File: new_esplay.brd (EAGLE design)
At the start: 100 x 50 mm, 96 parts, among them J3 AUDIO_JACK_3.5MM_KIT, Q1 1.1A/60V/600mΩ, T1 2n2222, T2 2n2222, T3 2n2222, U2 MIC5219 3.3V

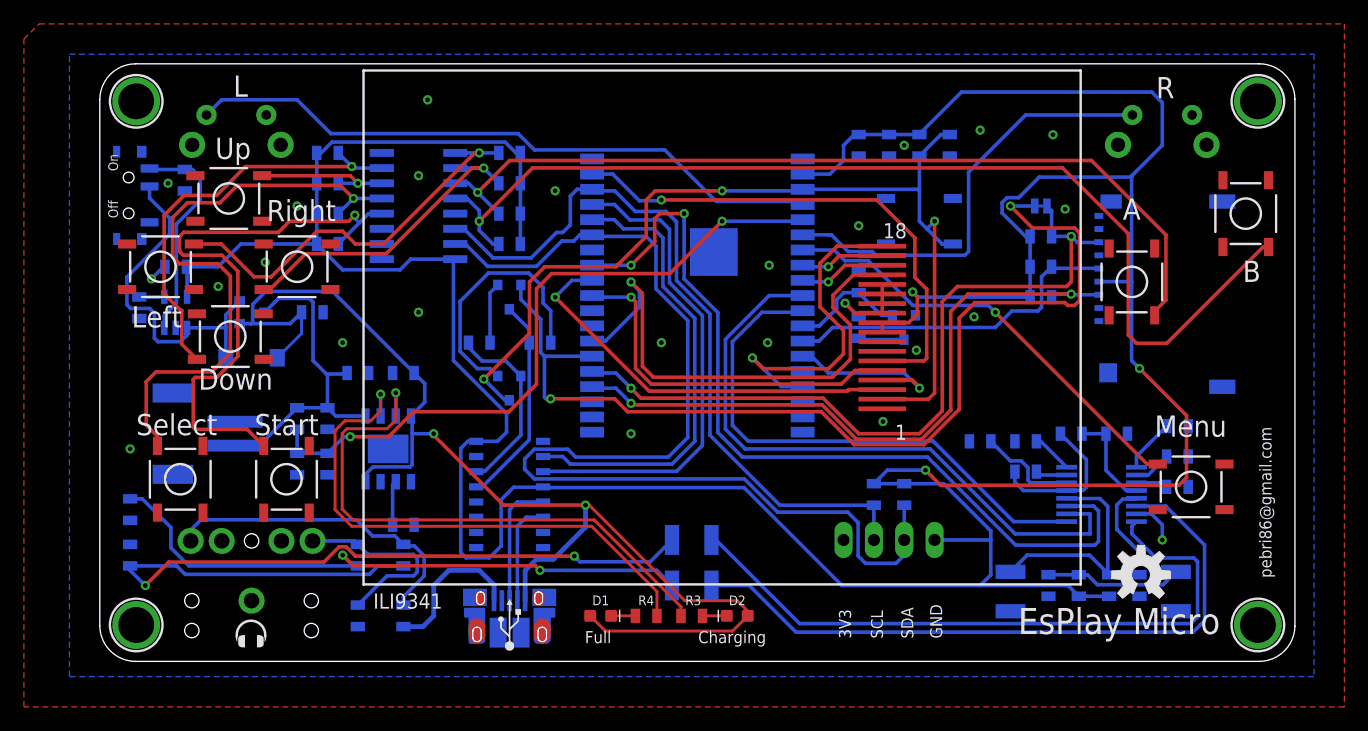
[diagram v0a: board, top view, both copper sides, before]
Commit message: Optimize vias and add amplifier
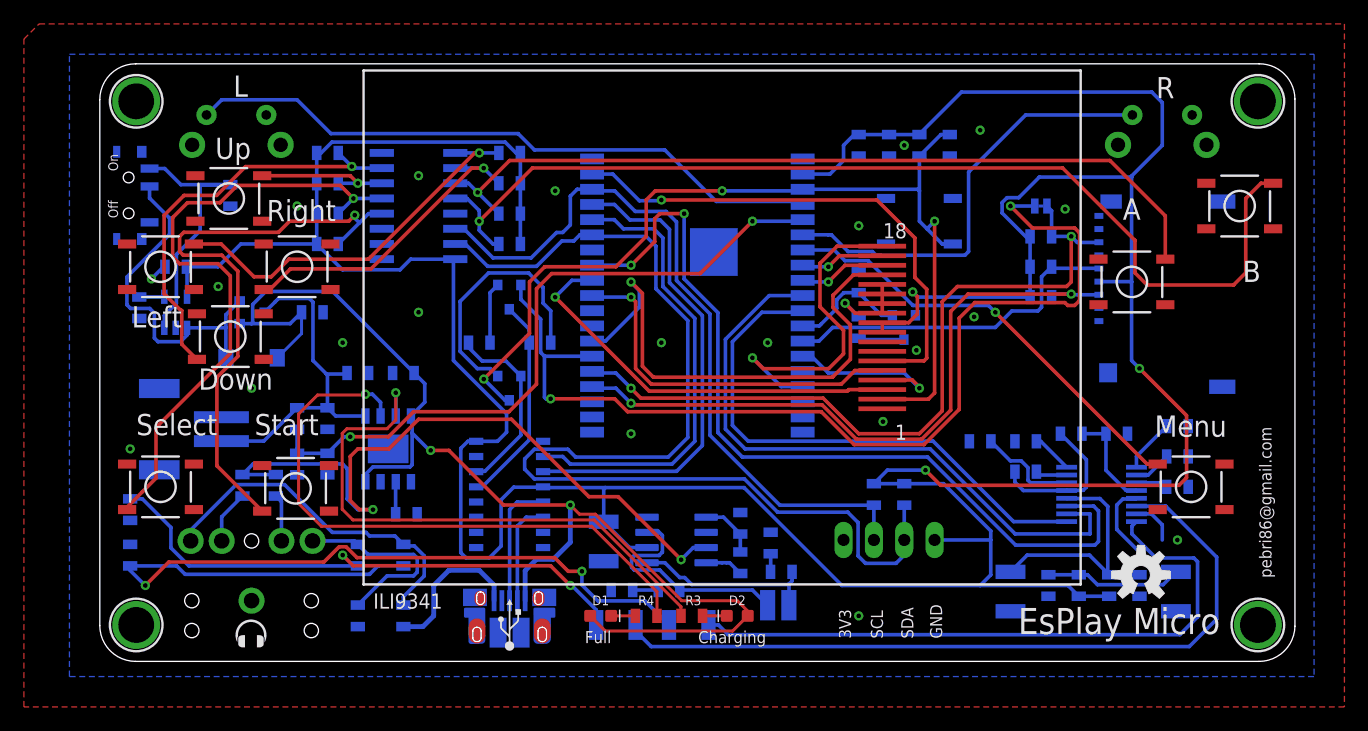
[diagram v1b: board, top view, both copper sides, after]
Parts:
- added C18: 47uF, SparkFun-Capacitors:EIA3528
- added C19: 10uF, SparkFun-Capacitors:0805
- added C20: 0.01uF, SparkFun-Capacitors:0805
- added C21, C24: 0.1uF, SparkFun-Capacitors:0805
- added R38, R41: 4,7, SparkFun-Resistors:0805
- added R39, R40: 100, SparkFun-Resistors:0805
- added SPK+, SPK-: (no value), wirepad:SMD1,27-2,54
- added U1: TDA2822MSOIC8, TDA2822M:SOIC127P600X175-8N
- moved C10 7.16 mm to (43.2, 3.05)
- moved C11 7.12 mm to (49.3, 3.05)
- moved R5 4.02 mm to (10.9, 39.0)
- moved S8 1.77 mm to (5.08, 14.6), turned to 0 degrees
- moved J2 1.20 mm to (6.48, 19.4)
- moved S7 1.08 mm to (16.4, 14.5), turned to 0 degrees
- moved R2 0.92 mm to (25.7, 12.3)
- moved S10 0.81 mm to (95.4, 38.1), turned to 180 degrees
- turned S9 to 180 degrees
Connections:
- removed net EXP: ESP32-WROVER.39
- new net N$15: J3.RSH, R39.1
- new net N$16: J3.TSH, R40.1
- new net N$17: R39.2, R40.2, U1.7
- new net N$23: C19.2, C20.1, U1.5
- new net N$30: C19.1, U1.8
- new net N$31: C24.1, SPK+.1, U1.1
- new net N$32: C21.1, SPK-.1, U1.3
- new net N$33: C21.2, R38.1
- new net N$34: C24.2, R41.1
- net 3V3: now also C18.A, U1.2
- net GND: now also C18.C, C20.2, ESP32-WROVER.39, J1.SHIELD, J1.SHIELD10, J1.SHIELD2, J1.SHIELD3, J1.SHIELD4, J1.SHIELD5, J1.SHIELD6, J1.SHIELD7, J1.SHIELD8, J1.SHIELD9, R38.2, R41.2, S10.2, S12.4, S3.2, S4.2, S5.2, S6.2, S7.2, S8.2, S9.2, U1.4, U1.6
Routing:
- net N$17: track 0.00 -> 59.4 mm, vias 0 -> 2
- net N$32: track 0.00 -> 19.1 mm
- net N$31: track 0.00 -> 15.6 mm
- net N$5: track 56.6 -> 64.3 mm
- net 3V3: track 309.3 -> 316.7 mm
- net N$3: track 46.1 -> 51.6 mm
- net N$23: track 0.00 -> 4.94 mm
- net N$7: track 18.4 -> 23.1 mm
- net N$16: track 0.00 -> 4.47 mm
- net N$18: track 52.6 -> 48.4 mm
- net A: track 73.1 -> 68.9 mm
- net N$15: track 0.00 -> 3.95 mm
- net N$30: track 0.00 -> 3.23 mm
- net SELECT: track 49.9 -> 52.8 mm
- net RDAC: track 26.9 -> 29.3 mm
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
